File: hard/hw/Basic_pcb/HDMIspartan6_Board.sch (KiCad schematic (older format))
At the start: 50 parts

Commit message: Actualizacion Power
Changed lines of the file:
@@
 LIBS:rj45_stamp
 LIBS:HDMIspartan6_Board-cache
-LIBS:pam8302-cache
 EELAYER 25 0
 EELAYER END
@@
 Comment4 ""
 $EndDescr
-$Sheet
-S 3200 3300 850  1350
-U 54B6445D
-F0 "spartan6" 60
-F1 "spartan6.sch" 60
-F2 "DS[0..7]" I R 4050 3550 60
-F3 "SNWE" I R 4050 3650 60
-F4 "SNRD" I R 4050 3750 60
-F5 "SNCS" I R 4050 3850 60
-F6 "SNWAIT" I R 4050 3950 60
-F7 "AS[0..13]" B R 4050 3450 60
-F8 "F_TCK" I R 4050 4200 60
-F9 "F_TDI" I R 4050 4500 60
-F10 "F_TDO" I R 4050 4400 60
-F11 "F_TMS" I R 4050 4300 60
-F12 "CLK_FPGA" I R 4050 4050 60
-$EndSheet
-Text Label 7000 3700 0    60   ~ 0
+Text Label 7000 1950 0    60   ~ 0
 P_TDO
-Text Label 4100 4500 0    60   ~ 0
+Text Label 4100 2750 0    60   ~ 0
 P_TDO
-Text Label 4100 4400 0    60   ~ 0
+Text Label 4100 2650 0    60   ~ 0
 F_TDO
 $Sheet
-S 7300 3150 1700 1250
+S 7300 1400 1700 1250
 U 555AB8C7
 F0 "serial_interface" 60
 F1 "serial_interface.sch" 60
-F2 "TXD" B L 7300 3400 60
-F3 "RXD" B L 7300 3300 60
-F4 "TCK" I L 7300 3800 60
-F5 "TDI" I L 7300 3700 60
-F6 "TDO" I L 7300 3600 60
-F7 "TMS" I L 7300 3900 60
-F8 "nTRST" I L 7300 3500 60
-F9 "nSRST" I L 7300 4000 60
+F2 "TXD" B L 7300 1650 60
+F3 "RXD" B L 7300 1550 60
+F4 "TCK" I L 7300 2050 60
+F5 "TDI" I L 7300 1950 60
+F6 "TDO" I L 7300 1850 60
+F7 "TMS" I L 7300 2150 60
+F8 "nTRST" I L 7300 1750 60
+F9 "nSRST" I L 7300 2250 60
 $EndSheet
 Wire Wire Line
-	6100 3400 7300 3400
-Wire Wire Line
-	6100 3500 7300 3500
-Wire Wire Line
-	6100 3800 7300 3800
-Wire Wire Line
-	6100 3900 7300 3900
-Wire Wire Line
-	6100 3300 7300 3300
-Wire Wire Line
-	6500 3800 6500 2950
-Wire Wire Line
-	6500 2950 4400 2950
-Wire Wire Line
-	4400 2950 4400 4200
-Wire Wire Line
-	4400 4200 4050 4200
-Connection ~ 6500 3800
-Wire Wire Line
-	6400 3900 6400 3050
-Wire Wire Line
-	6400 3050 4500 3050
-Wire Wire Line
-	4500 3050 4500 4300
-Wire Wire Line
-	4500 4300 4050 4300
-Connection ~ 6400 3900
-Wire Wire Line
-	4300 4400 4050 4400
-Wire Wire Line
-	4300 4500 4050 4500
-Wire Wire Line
-	7200 3700 7000 3700
-Wire Wire Line
-	6100 3700 7300 3700
-Text Label 7000 3600 0    60   ~ 0
+	6100 1650 7300 1650
+Wire Wire Line
+	6100 1750 7300 1750
+Wire Wire Line
+	6100 2050 7300 2050
+Wire Wire Line
+	6100 2150 7300 2150
+Wire Wire Line
+	6100 1550 7300 1550
+Wire Wire Line
+	6500 2050 6500 1200
+Wire Wire Line
+	6500 1200 4400 1200
+Wire Wire Line
+	4400 1200 4400 2450
+Wire Wire Line
+	4400 2450 4050 2450
+Connection ~ 6500 2050
+Wire Wire Line
+	6400 2150 6400 1300
+Wire Wire Line
+	6400 1300 4500 1300
+Wire Wire Line
+	4500 1300 4500 2550
+Wire Wire Line
+	4500 2550 4050 2550
+Connection ~ 6400 2150
+Wire Wire Line
+	4300 2650 4050 2650
+Wire Wire Line
+	4300 2750 4050 2750
+Wire Wire Line
+	7200 1950 7000 1950
+Wire Wire Line
+	6100 1950 7300 1950
+Text Label 7000 1850 0    60   ~ 0
 F_TDO
 Wire Wire Line
-	7300 3600 7000 3600
+	7300 1850 7000 1850
 $Comp
 L CONN_1 TH1
@@
 $EndComp
 $Sheet
-S 8100 4800 950  900
+S 7300 3200 950  900
 U 5898EE54
 F0 "Audio" 60
 F1 "Audio.sch" 60
+F2 "VCC" I L 7300 3400 60
+F3 "GND" I L 7300 3900 60
+F4 "~SD" I L 7300 3650 60
 $EndSheet
 $Sheet
-S 5600 4850 1000 950
+S 3200 1550 850  1350
+U 54B6445D
+F0 "spartan6" 60
+F1 "spartan6.sch" 60
+F2 "F_TCK" I R 4050 2450 60
+F3 "F_TDI" I R 4050 2750 60
+F4 "F_TDO" I R 4050 2650 60
+F5 "F_TMS" I R 4050 2550 60
+$EndSheet
+$Sheet
+S 3100 3300 1000 950
 U 58991CBD
 F0 "Power" 60

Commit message: Datasheets
By Rubén
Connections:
- wire segments 23 -> 20
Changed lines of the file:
@@
 $EndSheet
-Wire Wire Line
-	6100 1650 7300 1650
-Wire Wire Line
-	6100 1750 7300 1750
 Wire Wire Line
 	6100 2050 7300 2050
@@
 	6100 2150 7300 2150
 Wire Wire Line
-	6100 1550 7300 1550
-Wire Wire Line
 	6500 2050 6500 1200

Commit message: Actualizacion Raiz
por Rubén
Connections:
- net labels removed: F_TDO, P_TDO
- wire segments 20 -> 11
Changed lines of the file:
@@
 Comment4 ""
 $EndDescr
-Text Label 7000 1950 0    60   ~ 0
-P_TDO
-Text Label 4100 2750 0    60   ~ 0
-P_TDO
-Text Label 4100 2650 0    60   ~ 0
-F_TDO
 $Sheet
-S 7300 1400 1700 1250
+S 7300 1400 1500 1450
 U 555AB8C7
 F0 "serial_interface" 60
@@
 F6 "TDO" I L 7300 1850 60
 F7 "TMS" I L 7300 2150 60
-F8 "nTRST" I L 7300 1750 60
-F9 "nSRST" I L 7300 2250 60
+F8 "nTRST" I L 7300 2500 60
+F9 "nSRST" I L 7300 2400 60
 $EndSheet
-Wire Wire Line
-	6100 2050 7300 2050
-Wire Wire Line
-	6100 2150 7300 2150
-Wire Wire Line
-	6500 2050 6500 1200
-Wire Wire Line
-	6500 1200 4400 1200
-Wire Wire Line
-	4400 1200 4400 2450
-Wire Wire Line
-	4400 2450 4050 2450
-Connection ~ 6500 2050
-Wire Wire Line
-	6400 2150 6400 1300
-Wire Wire Line
-	6400 1300 4500 1300
-Wire Wire Line
-	4500 1300 4500 2550
-Wire Wire Line
-	4500 2550 4050 2550
-Connection ~ 6400 2150
-Wire Wire Line
-	4300 2650 4050 2650
-Wire Wire Line
-	4300 2750 4050 2750
-Wire Wire Line
-	7200 1950 7000 1950
-Wire Wire Line
-	6100 1950 7300 1950
-Text Label 7000 1850 0    60   ~ 0
-F_TDO
-Wire Wire Line
-	7300 1850 7000 1850
 $Comp
 L CONN_1 TH1
@@
 $EndComp
 $Sheet
-S 7300 3200 950  900
+S 7300 3450 950  900
 U 5898EE54
 F0 "Audio" 60
 F1 "Audio.sch" 60
-F2 "VCC" I L 7300 3400 60
-F3 "GND" I L 7300 3900 60
-F4 "~SD" I L 7300 3650 60
+F2 "~SD" I L 7300 3700 60
 $EndSheet
 $Sheet
-S 3200 1550 850  1350
+S 4950 1400 900  1450
 U 54B6445D
 F0 "spartan6" 60
 F1 "spartan6.sch" 60
-F2 "F_TCK" I R 4050 2450 60
-F3 "F_TDI" I R 4050 2750 60
-F4 "F_TDO" I R 4050 2650 60
-F5 "F_TMS" I R 4050 2550 60
+F2 "F_TCK" I R 5850 2050 60
+F3 "F_TDI" I R 5850 1950 60
+F4 "F_TDO" I R 5850 1850 60
+F5 "F_TMS" I R 5850 2150 60
+F6 "F_RXD" I R 5850 1550 60
+F7 "F_TXD" I R 5850 1650 60
 $EndSheet
 $Sheet
-S 3100 3300 1000 950
+S 4850 3450 1000 950
 U 58991CBD
 F0 "Power" 60
 F1 "Power.sch" 60
 $EndSheet
+Wire Wire Line
+	7300 1850 5850 1850
+Wire Wire Line
+	7300 1950 5850 1950
+Wire Wire Line
+	7300 2050 5850 2050
+Wire Wire Line
+	7300 2150 5850 2150
+Wire Wire Line
+	5850 1550 7300 1550
+Wire Wire Line
+	7300 1650 5850 1650
 $EndSCHEMATC

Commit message: Actualización Raiz
by Rubén
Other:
- note added: "PENDIENTES:\n\n>>> IMPLEMENTAR REGLAS DEL FABRICANTE <<<\n\n- Boton RST\n- Huella L3\n- Todos los conectores de 2.54mm (?), menos LVDS.\n- Referenciar elementos importantes segun fabricante y DigiKey\n- Conectar SD a FPGA, preguntar diodo de proteccion\n- Huella TPS63070\n- Reorganizar PinOut"
- moved on the sheet: TH1, TH10, TH11, TH12, TH13, TH14, TH15, TH16, TH17, TH18, TH19, TH2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

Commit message: todas las huellas
by Ruben
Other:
- note added: "PENDIENTES:\n\n>>> IMPLEMENTAR REGLAS DEL FABRICANTE <<<\n\n- Boton RST\n- Todos los conectores de 2.54mm (?), menos LVDS.\n- Referenciar elementos importantes segun fabricante y DigiKey\n- Conectar SD a FPGA, preguntar diodo de proteccion\n- Reorganizar PinOut"
- note removed: "PENDIENTES:\n\n>>> IMPLEMENTAR REGLAS DEL FABRICANTE <<<\n\n- Boton RST\n- Huella L3\n- Todos los conectores de 2.54mm (?), menos LVDS.\n- Referenciar elementos importantes segun fabricante y DigiKey\n- Conectar SD a FPGA, preguntar diodo de proteccion\n- Huella TPS63070\n- Reorganizar PinOut"
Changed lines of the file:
@@
 $EndDescr
 $Sheet
-S 6650 1250 1500 1450
+S 8150 1950 1100 1400
 U 555AB8C7
 F0 "serial_interface" 60
 F1 "serial_interface.sch" 60
-F2 "TXD" B L 6650 1600 60
-F3 "RXD" B L 6650 1500 60
-F4 "TCK" I L 6650 2050 60
-F5 "TDI" I L 6650 1950 60
-F6 "TDO" I L 6650 1850 60
-F7 "TMS" I L 6650 2150 60
-F8 "USB_5V" I L 6650 2550 60
+F2 "TXD" B L 8150 2300 60
+F3 "RXD" B L 8150 2200 60
+F4 "TCK" I L 8150 2750 60
+F5 "TDI" I L 8150 2650 60
+F6 "TDO" I L 8150 2550 60
+F7 "TMS" I L 8150 2850 60
+F8 "USB_5V" I L 8150 3100 60
 $EndSheet
 $Comp
@@
 $EndComp
 $Sheet
-S 4250 3150 950  900
+S 5800 3800 900  600
 U 5898EE54
 F0 "Audio" 60
 F1 "Audio.sch" 60
-F2 "~SD" I L 4250 3400 60
+F2 "~SD" I R 6700 4100 60
 $EndSheet
 $Sheet
-S 4300 1250 900  1450
+S 5750 1950 950  1400
 U 54B6445D
 F0 "spartan6" 60
 F1 "spartan6.sch" 60
-F2 "F_TCK" I R 5200 2050 60
-F3 "F_TDI" I R 5200 1950 60
-F4 "F_TDO" I R 5200 1850 60
-F5 "F_TMS" I R 5200 2150 60
-F6 "F_RXD" I R 5200 1500 60
-F7 "F_TXD" I R 5200 1600 60
+F2 "F_TCK" I R 6700 2750 60
+F3 "F_TDI" I R 6700 2650 60
+F4 "F_TDO" I R 6700 2550 60
+F5 "F_TMS" I R 6700 2850 60
+F6 "F_RXD" I R 6700 2200 60
+F7 "F_TXD" I R 6700 2300 60
+F8 "F_~SD" I R 6700 3100 60
 $EndSheet
 $Sheet
-S 6650 3150 1000 950
+S 8150 3800 1100 600
 U 58991CBD
 F0 "Power" 60
 F1 "Power.sch" 60
-F2 "USBVCC" I L 6650 3350 60
+F2 "USBVCC" I L 8150 4100 60
 $EndSheet
 Wire Wire Line
-	6650 1850 5200 1850
-Wire Wire Line
-	6650 1950 5200 1950
-Wire Wire Line
-	6650 2050 5200 2050
-Wire Wire Line
-	6650 2150 5200 2150
-Wire Wire Line
-	5200 1500 6650 1500
-Wire Wire Line
-	6650 1600 5200 1600
-Wire Wire Line
-	6650 3350 6450 3350
-Wire Wire Line
-	6450 3350 6450 2550
-Wire Wire Line
-	6450 2550 6650 2550
+	8150 2550 6700 2550
+Wire Wire Line
+	8150 2650 6700 2650
+Wire Wire Line
+	8150 2750 6700 2750
+Wire Wire Line
+	8150 2850 6700 2850
+Wire Wire Line
+	6700 2200 8150 2200
+Wire Wire Line
+	8150 2300 6700 2300
 Text Notes 950  3450 0    60   ~ 0
-PENDIENTES:\n\n>>> IMPLEMENTAR REGLAS DEL FABRICANTE <<<\n\n- Boton RST\n- Huella L3\n- Todos los conectores de 2.54mm (?), menos LVDS.\n- Referenciar elementos importantes segun fabricante y DigiKey\n- Conectar SD a FPGA, preguntar diodo de proteccion\n- Huella TPS63070\n- Reorganizar PinOut
+PENDIENTES:\n\n>>> IMPLEMENTAR REGLAS DEL FABRICANTE <<<\n\n- Boton RST\n- Todos los conectores de 2.54mm (?), menos LVDS.\n- Referenciar elementos importantes segun fabricante y DigiKey\n- Conectar SD a FPGA, preguntar diodo de proteccion\n- Reorganizar PinOut
 Wire Notes Line
 	750  2200 750  3700
@@
 Wire Notes Line
 	4000 2200 750  2200
+Wire Wire Line
+	7950 4100 8150 4100
+Wire Wire Line
+	6700 3100 6900 3100
+Wire Wire Line
+	6900 3100 6900 4100
+Wire Wire Line
+	6900 4100 6700 4100
+Wire Wire Line
+	7950 4100 7950 3100
+Wire Wire Line
+	7950 3100 8150 3100
 $EndSCHEMATC

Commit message: Organizando PIN OUT vr.:0.1
by Ruben
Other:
- note added: "PENDIENTES:\n\n>>> IMPLEMENTAR REGLAS DEL FABRICANTE <<<\n\n- Reorganizar PinOut"
- note removed: "PENDIENTES:\n\n>>> IMPLEMENTAR REGLAS DEL FABRICANTE <<<\n\n- Boton RST\n- Todos los conectores de 2.54mm (?), menos LVDS.\n- Referenciar elementos importantes segun fabricante y DigiKey\n- Conectar SD a FPGA, preguntar diodo de proteccion\n- Reorganizar PinOut"
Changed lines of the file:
@@
 	8150 2300 6700 2300
 Text Notes 950  3450 0    60   ~ 0
-PENDIENTES:\n\n>>> IMPLEMENTAR REGLAS DEL FABRICANTE <<<\n\n- Boton RST\n- Todos los conectores de 2.54mm (?), menos LVDS.\n- Referenciar elementos importantes segun fabricante y DigiKey\n- Conectar SD a FPGA, preguntar diodo de proteccion\n- Reorganizar PinOut
+PENDIENTES:\n\n>>> IMPLEMENTAR REGLAS DEL FABRICANTE <<<\n\n- Reorganizar PinOut
 Wire Notes Line
 	750  2200 750  3700

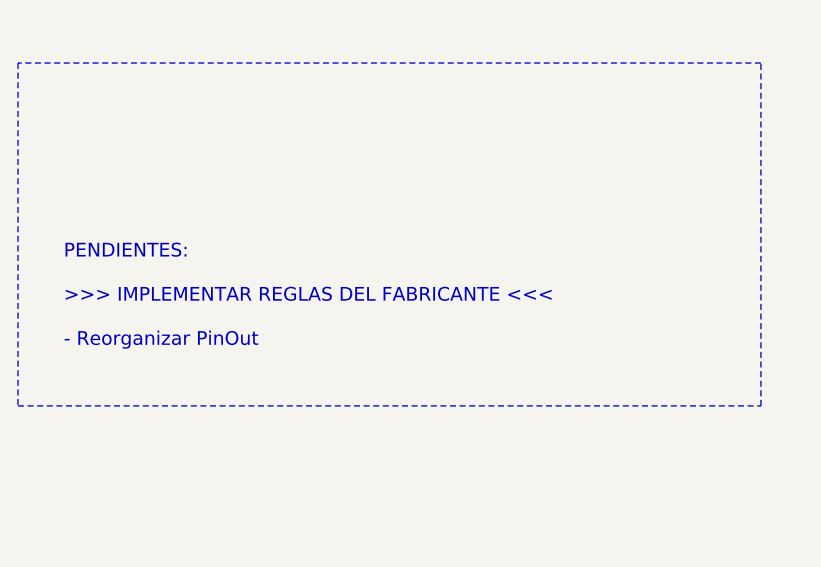
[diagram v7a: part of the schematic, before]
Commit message: Alimentacion Pantalla
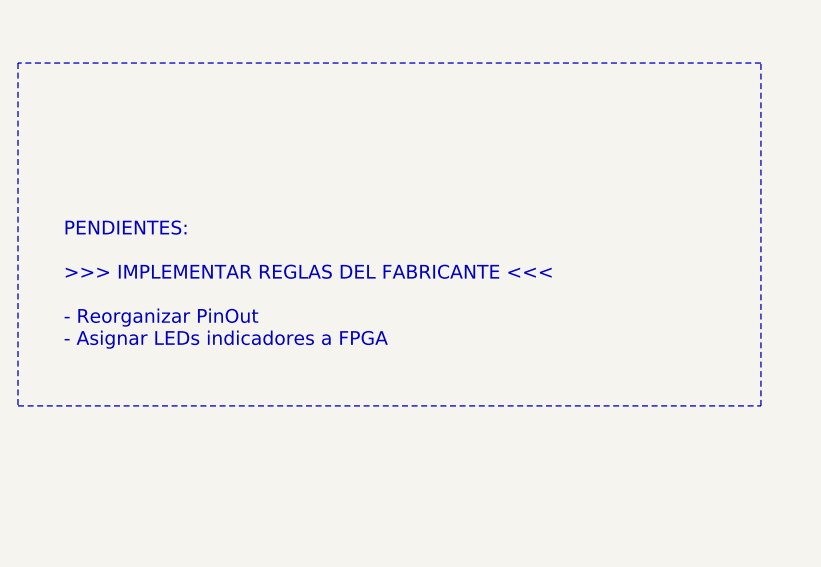
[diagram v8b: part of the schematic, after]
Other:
- note added: "PENDIENTES:\n\n>>> IMPLEMENTAR REGLAS DEL FABRICANTE <<<\n\n- Reorganizar PinOut\n- Asignar LEDs indicadores a FPGA"
- note removed: "PENDIENTES:\n\n>>> IMPLEMENTAR REGLAS DEL FABRICANTE <<<\n\n- Reorganizar PinOut"
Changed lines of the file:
@@
 	8150 2300 6700 2300
 Text Notes 950  3450 0    60   ~ 0
-PENDIENTES:\n\n>>> IMPLEMENTAR REGLAS DEL FABRICANTE <<<\n\n- Reorganizar PinOut
+PENDIENTES:\n\n>>> IMPLEMENTAR REGLAS DEL FABRICANTE <<<\n\n- Reorganizar PinOut\n- Asignar LEDs indicadores a FPGA
 Wire Notes Line
 	750  2200 750  3700
